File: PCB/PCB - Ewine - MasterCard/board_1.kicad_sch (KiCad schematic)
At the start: 8 parts, among them J6 DebugConnector, SW1 reset_btn, U3 STM32WB55RGV7, Y1 CM8V-T1A-0.3-32.768KHZ-12.5PF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

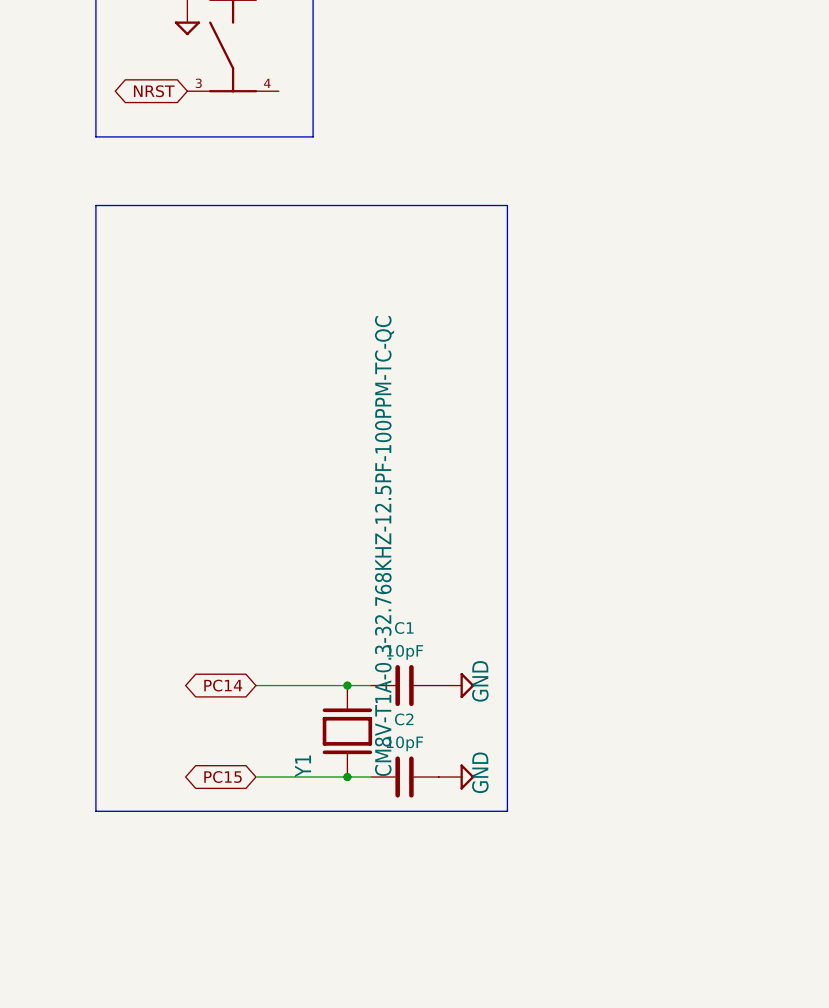
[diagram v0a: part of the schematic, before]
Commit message: pcb master card ok + il reste à mettre les pins des capteurs restants
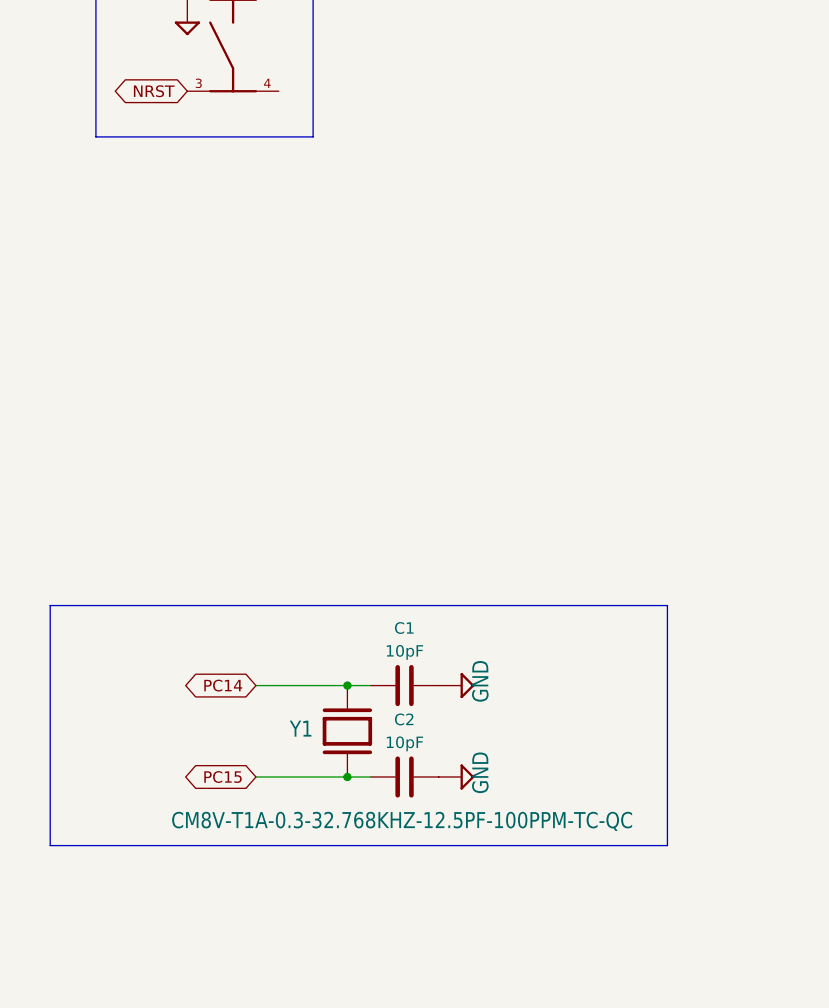
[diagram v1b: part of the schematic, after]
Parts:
- C1, C2: footprint Capacitor_SMD:C_0402_1005Metric -> Capacitor_SMD:C_0603_1608Metric
- R2: footprint Resistor_SMD:R_0402_1005Metric -> Resistor_SMD:R_0603_1608Metric
- SJ6: footprint board:PAD-JUMPER-2-NC_BY_PASTE_YES_SILK -> Jumper:SolderJumper-2_P1.3mm_Bridged_RoundedPad1.0x1.5mm
- SW1: footprint SW_434331013822 -> Library:STM32WB55RG_ResetButton
- U3: footprint STM32WB55RGV7:QFN40P800X800X100-69N -> Library:STM32WB55RG
- Y1: footprint board:XTAL_CM8V-T1A-0.3-32.768KHZ-12.5PF-100PPM-TC-QC -> Library:STM32WB55RG_XTAL
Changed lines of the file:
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@@
     (fill (type none))
   )
-  (rectangle (start 48.26 97.79) (end 93.98 165.1)
+  (rectangle (start 43.18 142.24) (end 111.76 168.91)
     (stroke (width 0) (type default))
     (fill (type none))
@@
       (effects (font (size 1.27 1.27)))
     )
-    (property "Footprint" "Capacitor_SMD:C_0402_1005Metric" (at 86.36 160.3248 0)
+    (property "Footprint" "Capacitor_SMD:C_0603_1608Metric" (at 86.36 160.3248 0)
       (effects (font (size 1.27 1.27)) hide)
     )
@@
       (effects (font (size 1.27 1.27)))
     )
-    (property "Footprint" "Capacitor_SMD:C_0402_1005Metric" (at 86.36 150.1648 0)
+    (property "Footprint" "Capacitor_SMD:C_0603_1608Metric" (at 86.36 150.1648 0)
       (effects (font (size 1.27 1.27)) hide)
     )
@@
       (effects (font (size 1.27 1.27)))
     )
-    (property "Footprint" "STM32WB55RGV7:QFN40P800X800X100-69N" (at 242.57 30.48 0)
+    (property "Footprint" "Library:STM32WB55RG" (at 242.57 30.48 0)
       (effects (font (size 1.27 1.27)) (justify bottom) hide)
     )
@@
       (effects (font (size 1.778 1.5113)) (justify left bottom))
     )
-    (property "Footprint" "board:PAD-JUMPER-2-NC_BY_PASTE_YES_SILK" (at 160.02 119.38 0)
+    (property "Footprint" "Jumper:SolderJumper-2_P1.3mm_Bridged_RoundedPad1.0x1.5mm" (at 160.02 119.38 0)
       (effects (font (size 1.27 1.27)) hide)
     )
@@
       (effects (font (size 1.27 1.27)))
     )
-    (property "Footprint" "STM32WB55RGV7:QFN40P800X800X100-69N" (at 247.65 99.06 0)
+    (property "Footprint" "Library:STM32WB55RG" (at 247.65 99.06 0)
       (effects (font (size 1.27 1.27)) (justify bottom) hide)
     )
@@
       (effects (font (size 1.27 1.27)))
     )
-    (property "Footprint" "SW_434331013822" (at 63.5 80.01 0)
+    (property "Footprint" "Library:STM32WB55RG_ResetButton" (at 63.5 80.01 0)
       (effects (font (size 1.27 1.27)) (justify bottom) hide)
     )
@@
   (symbol (lib_id "board-eagle-import:CM8V-T1A-0.3-32.768KHZ-12.5PF-100PPM-TC-QC") (at 76.2 156.21 90) (unit 1)
     (in_bom yes) (on_board yes) (dnp no)
-    (property "Reference" "Y1" (at 72.3841 161.2978 0)
+    (property "Reference" "Y1" (at 72.39 154.94 90)
       (effects (font (size 1.7807 1.5135)) (justify left bottom))
     )
-    (property "Value" "CM8V-T1A-0.3-32.768KHZ-12.5PF-100PPM-TC-QC" (at 81.2943 161.3043 0)
+    (property "Value" "CM8V-T1A-0.3-32.768KHZ-12.5PF-100PPM-TC-QC" (at 107.95 165.1 90)
       (effects (font (size 1.783 1.5155)) (justify left bottom))
     )
-    (property "Footprint" "board:XTAL_CM8V-T1A-0.3-32.768KHZ-12.5PF-100PPM-TC-QC" (at 76.2 156.21 0)
+    (property "Footprint" "Library:STM32WB55RG_XTAL" (at 76.2 156.21 0)
       (effects (font (size 1.27 1.27)) hide)
     )
@@
       (effects (font (size 1.27 1.27)))
     )
-    (property "Footprint" "STM32WB55RGV7:QFN40P800X800X100-69N" (at 236.22 176.53 0)
+    (property "Footprint" "Library:STM32WB55RG" (at 236.22 176.53 0)
       (effects (font (size 1.27 1.27)) (justify bottom) hide)
     )
@@
       (effects (font (size 1.27 1.27)))
     )
-    (property "Footprint" "Resistor_SMD:R_0402_1005Metric" (at 158.75 122.682 90)
-      (effects (font (size 1.27 1.27)) hide)
-    )
+    (property "Footprint" "Resistor_SMD:R_0603_1608Metric" (at 158.75 122.682 90)
+      (effects (font (size 1.27 1.27)) hide)
+    )
